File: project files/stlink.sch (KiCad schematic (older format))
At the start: 50 parts

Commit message: update
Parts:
- added C? (x2): 22uF, symbol Device:CP
- added C? (x2): 100nF, symbol Device:C
- added D?: BAT60A, Diode_SMD:D_SOD-323, symbol Diode:BAT60A
- added D?: Green, symbol Device:LED
- added F?: 1A, symbol Device:Polyfuse
- added J?: SWIM, symbol Connector_Generic:Conn_01x04
- added JP?: Jumper_2_Open, symbol Jumper:Jumper_2_Open
- added R?: 1K, symbol Device:R
- added U?: AMS1117-3.3, Package_TO_SOT_SMD:SOT-223-3_TabPin2, symbol Regulator_Linear:AMS1117-3.3
- D?: value Green -> Power
- J?: value STDC14 -> SWD
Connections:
- wire segments 131 -> 151
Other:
- note added: "Compatible with 10-pin\nCortex Debug Connector"
- note added: "Don't solder\nresistor for PC14!"
- note added: "ERNI SWIM"
- note added: "Inner Wiring Of Interfaces"
- note added: "Just in case there is a need\nto power target from ST-Link"
- note added: "Labels ended with "h" are conected to headers"
- note added: "MMBT9013 (SOT-23) is pinout compatible with:\n- MMBT2222\n- MMBT3904\n- BC847\n"
- note added: "STDC-14 as SWD"
- note added: "Target Programming Connectors"
- note removed: "Don't solder this one!"
- moved on the sheet: C?, D?, J?, Q?, R?, U?

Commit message: update
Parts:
- removed D?: Red, symbol Device:LED
- removed D?: Green, symbol Device:LED
- removed J?: SWIM, symbol Connector_Generic:Conn_01x04
- removed SW?: Reset, symbol Switch:SW_Push
- removed SW?: Boot0, symbol Switch:SW_Push
- added D2: LED_Dual_CACA, LED_SMD:LED_Avago_PLCC4_3.2x2.8mm_CW, symbol Device:LED_Dual_CACA
- added J2: Sides, Package_DIP:DIP-24_W15.24mm_Socket, symbol Connector_Generic:Conn_02x12_Counter_Clockwise
- added R14: 100K, Resistor_SMD:R_0603_1608Metric_Pad1.05x0.95mm_HandSolder, symbol Device:R
- C1, C2, C3, C4, C5, C6: renamed from C?; footprint (none) -> Capacitor_SMD:C_0603_1608Metric
- C10, C12, C13, C14, C15, C8, C9: renamed from C?; footprint (none) -> Capacitor_SMD:C_0603_1608Metric_Pad1.05x0.95mm_HandSolder
- D3: renamed from D?; footprint (none) -> LED_SMD:LED_0603_1608Metric_Castellated
- J1: renamed from J?; footprint (none) -> Connector_USB:USB_C_Receptacle_Palconn_UTC16-G
- J3: renamed from J?; footprint (none) -> Connector_PinHeader_1.27mm:PinHeader_2x07_P1.27mm_Vertical_SMD
- R1, R10, R11, R12, R13, R15, R16, R17, R18, R19, R2, R20, R21, R22, R23, R24, R25, R26, R27, R28, R29, R3, R30, R31, R4, R5, R6, R7, R8, R9: renamed from R?; footprint (none) -> Resistor_SMD:R_0603_1608Metric_Pad1.05x0.95mm_HandSolder
- Y1: renamed from Y?; footprint (none) -> Crystal:Crystal_HC49-4H_Vertical
- gave numbers to parts that had none: 9
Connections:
- net labels added: BOOT_0h, T_Vref
- net labels removed: T_Vref_SWD, T_Vref_SWDh
- wire segments 151 -> 157
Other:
- note added: "Programming Connectors"
- note added: "STDC-14 as\nTarget SWD"
- note added: "Top LED : Green\nBottom : Red\nPackage : 3528 (PLCC-4)\nExample : LSG T676"
- note added: "Top-Right 4 pins:\nERNI SWIM connector"
- note removed: "ERNI SWIM"
- note removed: "STDC-14 as SWD"
- note removed: "Target Programming Connectors"
- moved on the sheet: C13, J3, R11, R13

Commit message: updates
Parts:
- removed C3: 20pF, Capacitor_SMD:C_0603_1608Metric, symbol Device:C
- removed J2: Sides, Package_DIP:DIP-24_W15.24mm_Socket, symbol Connector_Generic:Conn_02x12_Counter_Clockwise
- removed JP1: Jumper_2_Open, symbol Jumper:Jumper_2_Open
- removed R3: 100R, Resistor_SMD:R_0603_1608Metric_Pad1.05x0.95mm_HandSolder, symbol Device:R
- added J2: SELF, Connector_PinHeader_2.54mm:PinHeader_1x12_P2.54mm_Vertical, symbol Connector_Generic:Conn_01x12
- added J4: TARGET, Connector_PinHeader_2.54mm:PinHeader_1x12_P2.54mm_Vertical, symbol Connector_Generic:Conn_01x12
- C11, C7: footprint (none) -> Capacitor_Tantalum_SMD:CP_EIA-7343-30_AVX-N
- F1: footprint (none) -> Fuse:Fuse_1210_3225Metric
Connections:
- net +3V3: now also J2.2 (Pin_2), J2.9 (Pin_9)
- net +5V: now also J2.1 (Pin_1)
- net BOOT_0h: now also J2.8 (Pin_8)
- net GNDREF: now also J2.12 (Pin_12), J2.4 (Pin_4), J4.3 (Pin_3), J4.9 (Pin_9)
- net Self_NRSTh: now also J2.6 (Pin_6)
- net Self_RXh: now also J2.10 (Pin_10)
- net Self_SWDCLKh: now also J2.5 (Pin_5)
- net Self_SWDIOh: now also J2.3 (Pin_3)
- net Self_SWOh: now also J2.7 (Pin_7)
- net Self_TXh: now also J2.11 (Pin_11)
- net T_NRST_SWDh: now also J4.12 (Pin_12)
- net T_NRST_SWIMh: now also J4.4 (Pin_4)
- net T_SWDCLKh: now also J4.10 (Pin_10)
- net T_SWDIOh: now also J4.8 (Pin_8)
- net T_SWIMh: now also J4.2 (Pin_2)
- net T_SWOh: now also J4.11 (Pin_11)
- net T_VCP_RXh: now also J4.5 (Pin_5)
- net T_VCP_TXh: now also J4.6 (Pin_6)
- net T_Vref: now also J4.1 (Pin_1), J4.7 (Pin_7)
- no-connect marks 14 -> 15
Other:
- note removed: "Just in case there is a need\nto power target from ST-Link"

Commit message: ajfdlsa;jd;sakd
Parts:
- F1: footprint Fuse:Fuse_1210_3225Metric -> Fuse:Fuse_1206_3216Metric
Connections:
- net Self_SWDCLKh: now also J2.3 (Pin_3); no longer J2.5 (Pin_5)
- net Self_SWDIOh: now also J2.5 (Pin_5); no longer J2.3 (Pin_3)
- net T_NRST_SWDh: now also J4.11 (Pin_11); no longer J4.12 (Pin_12)
- net T_SWDCLKh: now also J4.8 (Pin_8); no longer J4.10 (Pin_10)
- net T_SWDIOh: now also J4.10 (Pin_10); no longer J4.8 (Pin_8)
- net T_SWOh: now also J4.12 (Pin_12); no longer J4.11 (Pin_11)
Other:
- note added: "Top-Right 4 pins:\nERNI SWIM connector\nBottom-Right Pins: \nNucleo SWD connector"
- note removed: "Top-Right 4 pins:\nERNI SWIM connector"
- moved on the sheet: R22, R28, R29, R30, R31
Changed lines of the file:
@@
 Text Label 10200 5500 2    50   ~ 0
 T_NRST_SWIM
-Wire Wire Line
-	10600 6400 10500 6400
-Wire Wire Line
-	10600 6300 10500 6300
-Wire Wire Line
-	10600 6200 10500 6200
-Wire Wire Line
-	10600 6100 10500 6100
-Wire Wire Line
-	10600 6000 10500 6000
-Text Label 10200 6400 2    50   ~ 0
+Text Label 10100 6400 2    50   ~ 0
 T_SWO
-Text Label 10200 6300 2    50   ~ 0
+Text Label 10100 6300 2    50   ~ 0
 T_SWDIO
-Text Label 10200 6200 2    50   ~ 0
+Text Label 10100 6200 2    50   ~ 0
 T_SWDCLK
-Text Label 10200 6100 2    50   ~ 0
+Text Label 10100 6100 2    50   ~ 0
 T_NRST_SWD
-Text Label 10500 6000 2    50   ~ 0
+Text Label 10400 6000 2    50   ~ 0
 T_Vref
 NoConn ~ 1150 5550
@@
 NoConn ~ 1150 5250
 $Comp
-L Device:R R31
-U 1 1 5E239BA0
-P 10350 6400
-F 0 "R31" V 10400 6550 50  0000 C CNN
-F 1 "22R" V 10350 6400 50  0000 C CNN
-F 2 "Resistor_SMD:R_0603_1608Metric_Pad1.05x0.95mm_HandSolder" V 10280 6400 50  0001 C CNN
-F 3 "~" H 10350 6400 50  0001 C CNN
-	1    10350 6400
-	0    1    -1   0
-$EndComp
-$Comp
-L Device:R R30
-U 1 1 5E241EAA
-P 10350 6300
-F 0 "R30" V 10400 6450 50  0000 C CNN
-F 1 "22R" V 10350 6300 50  0000 C CNN
-F 2 "Resistor_SMD:R_0603_1608Metric_Pad1.05x0.95mm_HandSolder" V 10280 6300 50  0001 C CNN
-F 3 "~" H 10350 6300 50  0001 C CNN
-	1    10350 6300
-	0    1    -1   0
-$EndComp
-$Comp
 L Device:R R29
 U 1 1 5E241FEE
-P 10350 6200
-F 0 "R29" V 10400 6350 50  0000 C CNN
-F 1 "22R" V 10350 6200 50  0000 C CNN
-F 2 "Resistor_SMD:R_0603_1608Metric_Pad1.05x0.95mm_HandSolder" V 10280 6200 50  0001 C CNN
-F 3 "~" H 10350 6200 50  0001 C CNN
-	1    10350 6200
+P 10250 6200
+F 0 "R29" V 10300 6400 50  0000 C CNN
+F 1 "22R" V 10250 6200 50  0000 C CNN
+F 2 "Resistor_SMD:R_0603_1608Metric_Pad1.05x0.95mm_HandSolder" V 10180 6200 50  0001 C CNN
+F 3 "~" H 10250 6200 50  0001 C CNN
+	1    10250 6200
 	0    1    -1   0
 $EndComp
@@
 L Device:R R28
 U 1 1 5E242103
-P 10350 6100
-F 0 "R28" V 10400 6250 50  0000 C CNN
-F 1 "22R" V 10350 6100 50  0000 C CNN
-F 2 "Resistor_SMD:R_0603_1608Metric_Pad1.05x0.95mm_HandSolder" V 10280 6100 50  0001 C CNN
-F 3 "~" H 10350 6100 50  0001 C CNN
-	1    10350 6100
+P 10250 6100
+F 0 "R28" V 10300 6300 50  0000 C CNN
+F 1 "22R" V 10250 6100 50  0000 C CNN
+F 2 "Resistor_SMD:R_0603_1608Metric_Pad1.05x0.95mm_HandSolder" V 10180 6100 50  0001 C CNN
+F 3 "~" H 10250 6100 50  0001 C CNN
+	1    10250 6100
 	0    1    -1   0
 $EndComp
@@
 L Device:R R22
 U 1 1 5E2426E2
-P 9700 6300
-F 0 "R22" V 9600 6300 50  0000 C CNN
-F 1 "100R" V 9700 6300 50  0000 C CNN
-F 2 "Resistor_SMD:R_0603_1608Metric_Pad1.05x0.95mm_HandSolder" V 9630 6300 50  0001 C CNN
-F 3 "~" H 9700 6300 50  0001 C CNN
-	1    9700 6300
+P 9600 6300
+F 0 "R22" V 9500 6300 50  0000 C CNN
+F 1 "100R" V 9600 6300 50  0000 C CNN
+F 2 "Resistor_SMD:R_0603_1608Metric_Pad1.05x0.95mm_HandSolder" V 9530 6300 50  0001 C CNN
+F 3 "~" H 9600 6300 50  0001 C CNN
+	1    9600 6300
 	0    -1   1    0
 $EndComp
-Text Label 9550 6300 2    50   ~ 0
+Text Label 9450 6300 2    50   ~ 0
 T_SWDIO_IN
 Text Label 1150 6350 2    50   ~ 0
@@
 T_SWDIO
 Wire Wire Line
-	10200 6300 9850 6300
+	10100 6300 9750 6300
 Text Label 2450 5650 0    50   ~ 0
 T_SWDCLK
@@
 Text GLabel 10700 3300 2    50   Output ~ 0
 T_SWDCLKh
-Text GLabel 8700 3750 2    50   Input ~ 0
+Text GLabel 8700 3850 2    50   Input ~ 0
 T_SWOh
 Text GLabel 10700 3600 2    50   Output ~ 0
@@
 F 0 "F1" V 1575 1100 50  0000 C CNN
 F 1 "1A" V 1666 1100 50  0000 C CNN
-F 2 "Fuse:Fuse_1210_3225Metric" H 1850 900 50  0001 L CNN
+F 2 "Fuse:Fuse_1206_3216Metric" H 1850 900 50  0001 L CNN
 F 3 "~" H 1800 1100 50  0001 C CNN
 	1    1800 1100
@@
 Text GLabel 8700 3350 2    50   Input ~ 0
 T_Vref
-Text GLabel 8700 3450 2    50   Output ~ 0
+Text GLabel 8700 3650 2    50   Output ~ 0
 T_SWDIOh
 $Comp
@@
 	-1   0    0    -1
 $EndComp
-Text GLabel 8700 3650 2    50   Output ~ 0
+Text GLabel 8700 3450 2    50   Output ~ 0
 T_SWDCLKh
-Text GLabel 8700 3850 2    50   Output ~ 0
+Text GLabel 8700 3750 2    50   Output ~ 0
 T_NRST_SWDh
 Text GLabel 8700 3150 2    50   Output ~ 0
@@
 	1    0    0    -1
 $EndComp
-Text GLabel 8000 2950 0    50   Input ~ 0
+Text GLabel 8000 3150 0    50   Input ~ 0
 Self_SWDIOh
 $Comp
@@
 	-1   0    0    -1
 $EndComp
-Text GLabel 8000 3150 0    50   Input ~ 0
+Text GLabel 8000 2950 0    50   Input ~ 0
 Self_SWDCLKh
 Text GLabel 8000 3250 0    50   Input ~ 0
@@
 Wire Wire Line
 	7750 2850 7750 2700
-Text Notes 8400 4100 0    50   ~ 0
-Top-Right 4 pins:\nERNI SWIM connector
+Text Notes 8450 4250 0    50   ~ 0
+Top-Right 4 pins:\nERNI SWIM connector\nBottom-Right Pins: \nNucleo SWD connector
 Wire Wire Line
 	6550 2200 6500 2200
@@
 	-1   0    0    -1
 $EndComp
+$Comp
+L Device:R R30
+U 1 1 5E241EAA
+P 10250 6300
+F 0 "R30" V 10300 6500 50  0000 C CNN
+F 1 "22R" V 10250 6300 50  0000 C CNN
+F 2 "Resistor_SMD:R_0603_1608Metric_Pad1.05x0.95mm_HandSolder" V 10180 6300 50  0001 C CNN
+F 3 "~" H 10250 6300 50  0001 C CNN
+	1    10250 6300
+	0    1    -1   0
+$EndComp
+$Comp
+L Device:R R31
+U 1 1 5E239BA0
+P 10250 6400
+F 0 "R31" V 10300 6600 50  0000 C CNN
+F 1 "22R" V 10250 6400 50  0000 C CNN
+F 2 "Resistor_SMD:R_0603_1608Metric_Pad1.05x0.95mm_HandSolder" V 10180 6400 50  0001 C CNN
+F 3 "~" H 10250 6400 50  0001 C CNN
+	1    10250 6400
+	0    1    -1   0
+$EndComp
+Wire Wire Line
+	10400 6100 10600 6100
+Wire Wire Line
+	10400 6200 10600 6200
+Wire Wire Line
+	10400 6300 10600 6300
+Wire Wire Line
+	10400 6400 10600 6400
+Wire Wire Line
+	10400 6000 10600 6000
 $EndSCHEMATC

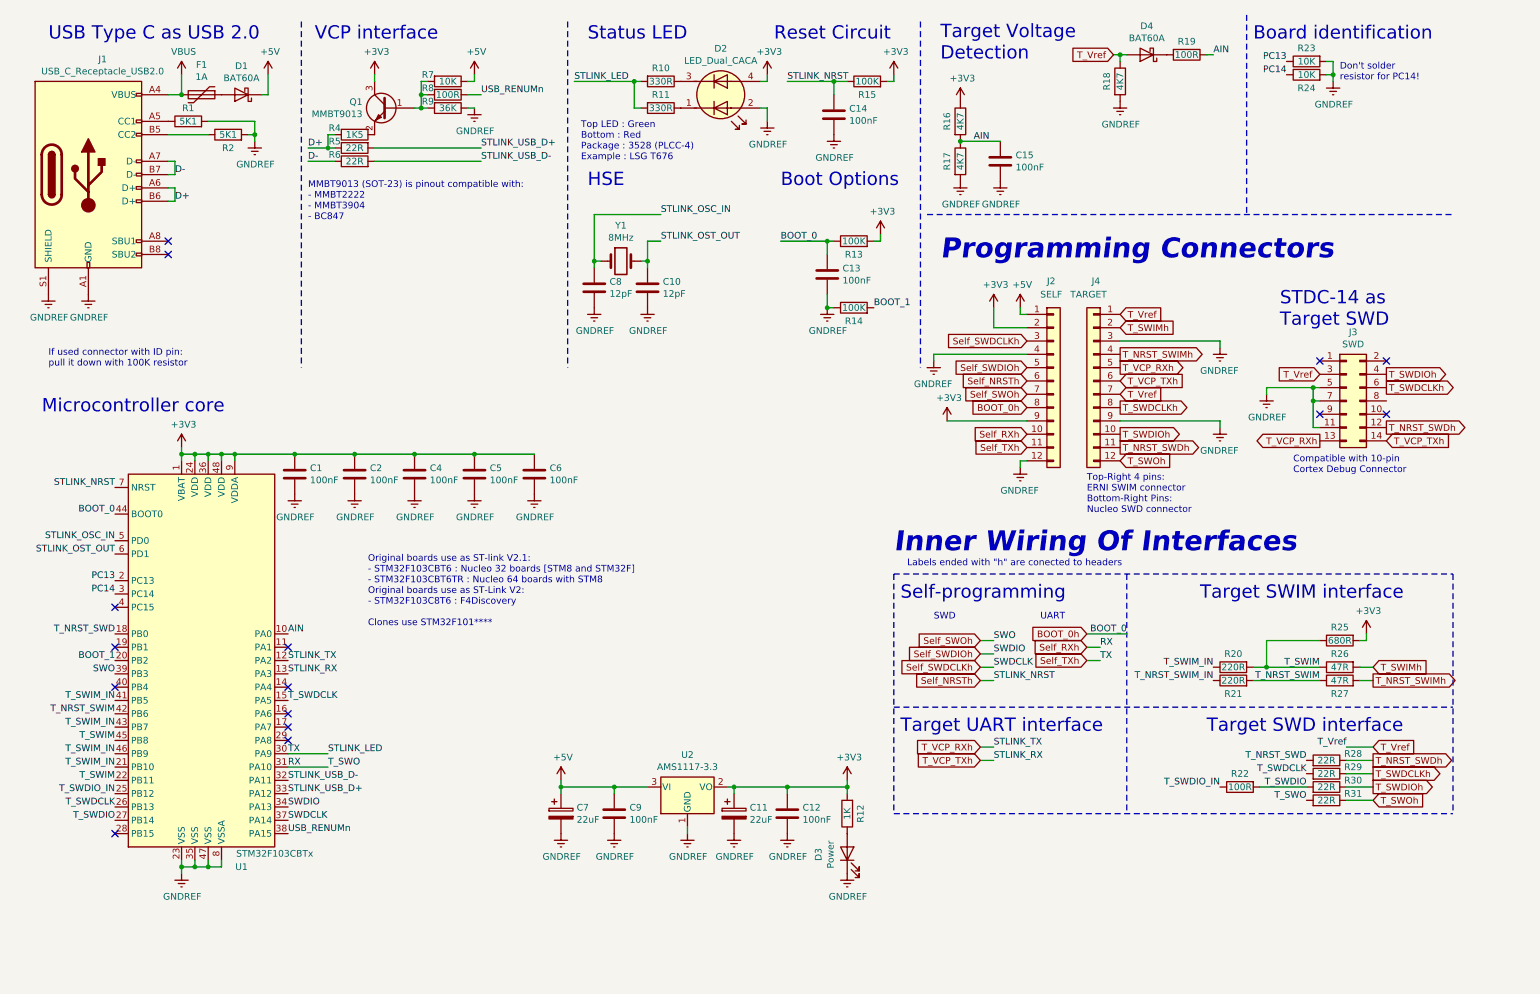
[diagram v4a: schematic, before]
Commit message: Added JTAG to STDC14
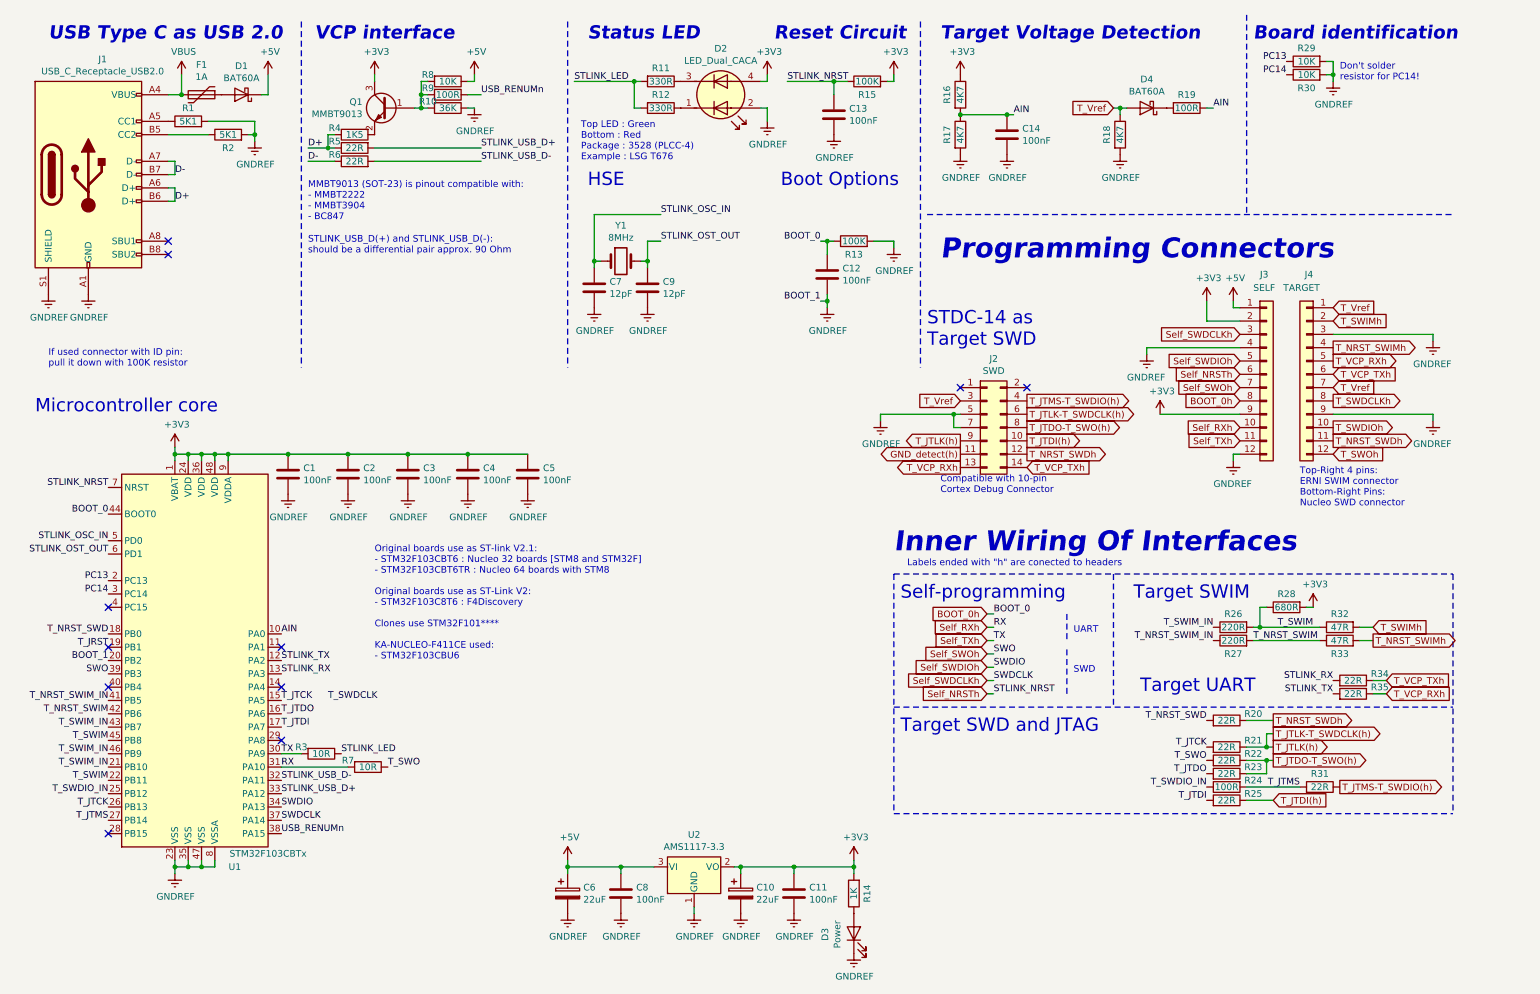
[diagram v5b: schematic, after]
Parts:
- removed R14: 100K, Resistor_SMD:R_0603_1608Metric_Pad1.05x0.95mm_HandSolder, symbol Device:R
- added R23, R25, R34, R35: 22R, Resistor_SMD:R_0603_1608Metric_Pad1.05x0.95mm_HandSolder, symbol Device:R
- added R3, R7: 10R, Resistor_SMD:R_0603_1608Metric_Pad1.05x0.95mm_HandSolder, symbol Device:R
- F1: footprint Fuse:Fuse_1206_3216Metric -> Fuse:Fuse_1812_4532Metric
- renumbered C11 to C10, C12 to C11, C13 to C12, C14 to C13, C15 to C14, C4 to C3, C5 to C4, C6 to C5, C7 to C6, C8 to C7, C9 to C8, C10 to C9, J3 to J2, J2 to J3, R9 to R10, R10 to R11, R11 to R12, R12 to R14, R28 to R20, R29 to R21, R31 to R22, R22 to R24, R20 to R26, R21 to R27, R25 to R28, R23 to R29, R24 to R30, R30 to R31, R26 to R32, R27 to R33, R7 to R8, R8 to R9
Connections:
- net BOOT_1 is gone; now on net GNDREF: U1.20 (PB2)
- net +3V3: no longer R13.2
- net GNDREF: now also R13.2; no longer J2.11 (Pin_11)
- net Self_RXh: now also R7.2; no longer R22.2
- net Self_TXh: now also R3.2; no longer R11.2, R12.2
- net T_NRST_SWIM_IN: now also U1.41 (PB5)
- net T_SWDCLK: no longer R21.2, U1.15 (PA5), U1.26 (PB13)
- net T_SWDCLKh: no longer J2.6 (Pin_6), R21.1
- net T_SWDIOh: no longer J2.4 (Pin_4), R31.1
- net T_SWIM_IN: no longer U1.41 (PB5)
- net T_SWOh: no longer R22.1
- net T_VCP_RXh: now also R35.1; no longer U1.12 (PA2)
- net T_VCP_TXh: now also R34.1; no longer U1.13 (PA3)
- net T_JTDO: now reaches U1.16 (PA6)
- net T_JTDO: now also R23.2
- net T_JTDI: now reaches U1.17 (PA7)
- net T_JTDI: now also R25.2
- net T_JRST: now reaches U1.19 (PB1)
- net T_JTDI(h): now reaches J2.10 (Pin_10)
- net T_JTDI(h): now also R25.1
- net T_JTDO-T_SWO(h): now reaches J2.8 (Pin_8)
- net T_JTDO-T_SWO(h): now also R22.1, R23.1
- net T_JTLK(h): now reaches J2.9 (Pin_9)
- net T_JTLK(h): now also J2.6 (Pin_6), R21.1
- net T_SWDIO renamed T_JTMS
- new net GND_detect(h): J2.11 (Pin_11)
- new net STLINK_LED: R11.2, R12.2, R3.1
- new net STLINK_RX: R34.2, U1.13 (PA3)
- new net STLINK_TX: R35.2, U1.12 (PA2)
- new net T_JTCK: R21.2, U1.15 (PA5), U1.26 (PB13)
- new net T_JTMS-T_SWDIO(h): J2.4 (Pin_4), R31.1
- new net T_SWO: R22.2, R7.1
- no-connect marks 15 -> 11
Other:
- note added: "Original boards use as ST-link V2.1:\n- STM32F103CBT6 : Nucleo 32 boards [STM8 and STM32F]\n- STM32F103CBT6TR : Nucleo 64 boards with STM8\n\nOriginal boards use as ST-Link V2:\n- STM32F103C8T6 : F4Discovery\n\nClones use STM32F101****\n\nKA-NUCLEO-F411CE used:\n- STM32F103CBU6"
- note added: "STLINK_USB_D(+) and STLINK_USB_D(-):\nshould be a differential pair approx. 90 Ohm"
- note added: "Target SWD and JTAG"
- note added: "Target SWIM"
- note added: "Target UART"
- note added: "Target Voltage Detection"
- note removed: "Original boards use as ST-link V2.1:\n- STM32F103CBT6 : Nucleo 32 boards [STM8 and STM32F]\n- STM32F103CBT6TR : Nucleo 64 boards with STM8\nOriginal boards use as ST-Link V2:\n- STM32F103C8T6 : F4Discovery\n\nClones use STM32F101****"
- note removed: "Target SWD interface"
- note removed: "Target SWIM interface"
- note removed: "Target UART interface"
- note removed: "Target Voltage\nDetection"
- moved on the sheet: C1, C10, C11, C14, C2, C3, C4, C5, C6, C8, D3, D4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
